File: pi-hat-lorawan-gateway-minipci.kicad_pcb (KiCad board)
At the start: 2 copper layers, 85 x 56 mm, 4 parts, among them Con1 RPi-Header-2x13, Con2 2041119-1

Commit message: Finalized project and generated all production files
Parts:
- added C1: 100n, Capacitors_Smd_0603:100nF_0603, F.Cu at (106.9, 109.5)
- added C2: 10uF, Capacitors_Smd_0603:10uF_10V_0603, F.Cu at (106.9, 106.9)
- added C3: 10uF, Capacitors_Smd_0603:10uF_10V_0603, F.Cu at (109.0, 77.6)
- added C4: 10uF, Capacitors_Smd_0603:10uF_10V_0603, F.Cu at (109.2, 83.4)
- added D1: KPG-1608SURKC-T, Diodes:LED_KPG-1608SURKC-T, F.Cu at (127.9, 81.8)
- added R3: 200R, Resistor_Smd_0603:200R_0603, F.Cu at (125.2, 81.8)
- added U1: LD39200, Linear:LD39200PU33R, F.Cu at (108.9, 80.5)
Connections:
- Con1 pad 10: (no net) -> /GPIO15(RXD)
- Con1 pad 11: (no net) -> /GPIO17(RTS)
- Con1 pad 12: (no net) -> /GPIO18(PWM)
- Con1 pad 13: (no net) -> /GPIO21
- Con1 pad 14: (no net) -> GND
- Con1 pad 15: (no net) -> /GPIO22
- Con1 pad 16: (no net) -> /GPIO23
- Con1 pad 17: (no net) -> 3V3
- Con1 pad 18: (no net) -> /GPIO24
- Con1 pad 19: (no net) -> /GPIO10(MOSI)
- Con1 pad 2: (no net) -> 5V
- Con1 pad 20: (no net) -> GND
- Con1 pad 21: (no net) -> /GPIO9(MISO)
- Con1 pad 22: (no net) -> /GPIO25
- Con1 pad 23: (no net) -> /GPIO11(SCLK)
- Con1 pad 24: (no net) -> /GPIO8(CE0)
- Con1 pad 25: (no net) -> GND
- Con1 pad 26: (no net) -> /GPIO7(CE1)
- Con1 pad 3: (no net) -> /GPIO0(SDA)
- Con1 pad 4: (no net) -> 5V
- Con1 pad 5: (no net) -> /GPIO1(SCL)
- Con1 pad 7: (no net) -> /GPIO4
- Con1 pad 8: (no net) -> /GPIO14(TXD)
- Con1 pad 9: (no net) -> GND
- Con2 pad 1: (no net) -> /GPIO4
- Con2 pad 10: (no net) -> /GPIO25
- Con2 pad 11: (no net) -> /GPIO14(TXD)
- Con2 pad 12: (no net) -> /GPIO10(MOSI)
- Con2 pad 13: (no net) -> /GPIO15(RXD)
- Con2 pad 14: (no net) -> /GPIO9(MISO)
- Con2 pad 16: (no net) -> /GPIO11(SCLK)
- Con2 pad 20: (no net) -> /GPIO8(CE0)
- Con2 pad 22: (no net) -> /GPIO22
- Con2 pad 23: (no net) -> /GPIO17(RTS)
- Con2 pad 25: (no net) -> /GPIO21
- Con2 pad 30: /MiniPci Express Module/I2C-SCL -> /GPIO1(SCL)
- Con2 pad 31: (no net) -> /GPIO18(PWM)
- Con2 pad 32: /MiniPci Express Module/I2C-SDA -> /GPIO0(SDA)
- Con2 pad 33: (no net) -> /GPIO7(CE1)
- Con2 pad 45: (no net) -> /GPIO23
- Con2 pad 8: (no net) -> /GPIO24
- R1 pad 2: /MiniPci Express Module/I2C-SCL -> /GPIO1(SCL)
- R2 pad 2: /MiniPci Express Module/I2C-SDA -> /GPIO0(SDA)
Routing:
- net 3V3: track 0.00 -> 107.1 mm, vias 0 -> 3
- net /GPIO7(CE1): track 0.00 -> 59.1 mm, vias 0 -> 2
- net /GPIO0(SDA): track 0.00 -> 52.6 mm, vias 0 -> 3
- net /GPIO1(SCL): track 0.00 -> 48.5 mm, vias 0 -> 3
- net /GPIO8(CE0): track 0.00 -> 46.6 mm, vias 0 -> 2
- net /GPIO23: track 0.00 -> 46.1 mm, vias 0 -> 2
- net /GPIO18(PWM): track 0.00 -> 38.5 mm
- net /GPIO25: track 0.00 -> 36.6 mm
- net /GPIO11(SCLK): track 0.00 -> 34.3 mm
- net /GPIO21: track 0.00 -> 33.9 mm, vias 0 -> 2
- net /GPIO9(MISO): track 0.00 -> 32.5 mm
- net /GPIO10(MOSI): track 0.00 -> 32.0 mm
- net /GPIO17(RTS): track 0.00 -> 31.9 mm
- net /GPIO22: track 0.00 -> 31.1 mm
- net /GPIO15(RXD): track 0.00 -> 28.1 mm, vias 0 -> 2
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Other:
- rule via_min_drill: 0.5 -> 0.4

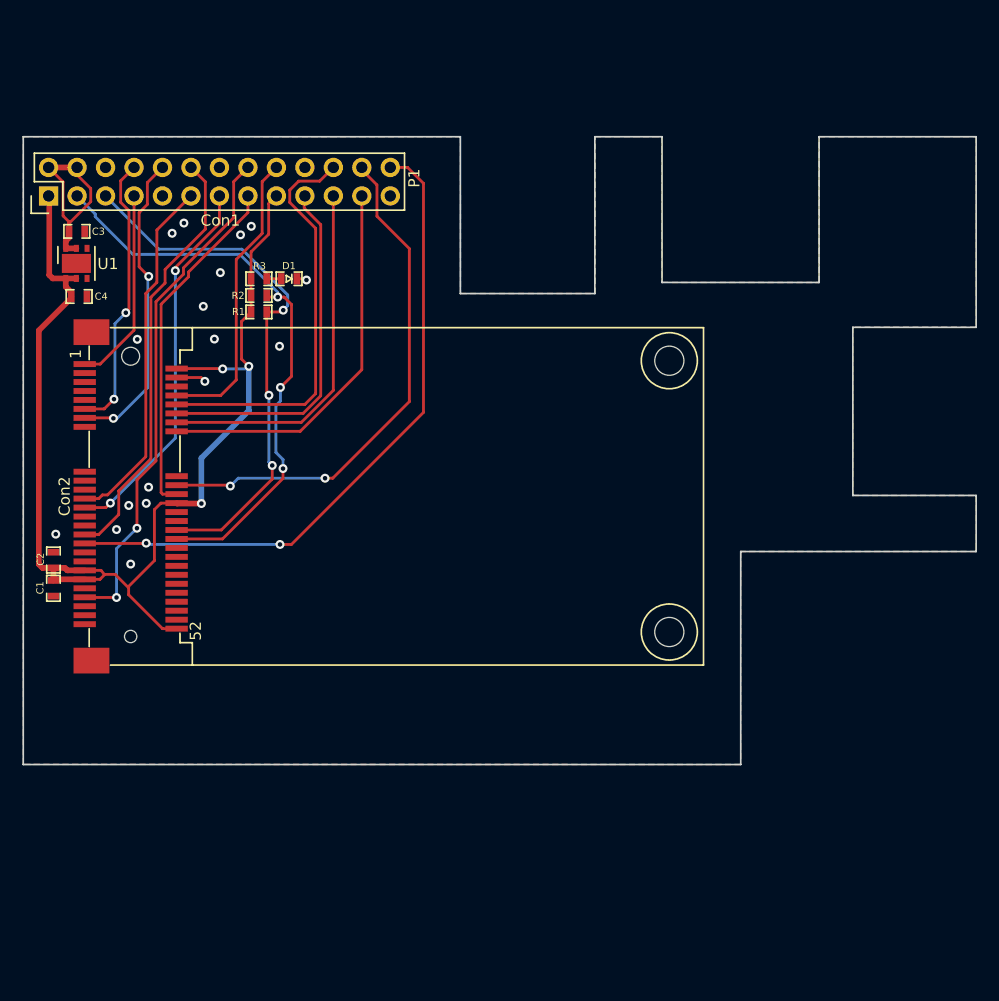
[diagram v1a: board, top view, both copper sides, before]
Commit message: Applied Issue 1, performed valid SPI connection to RPi
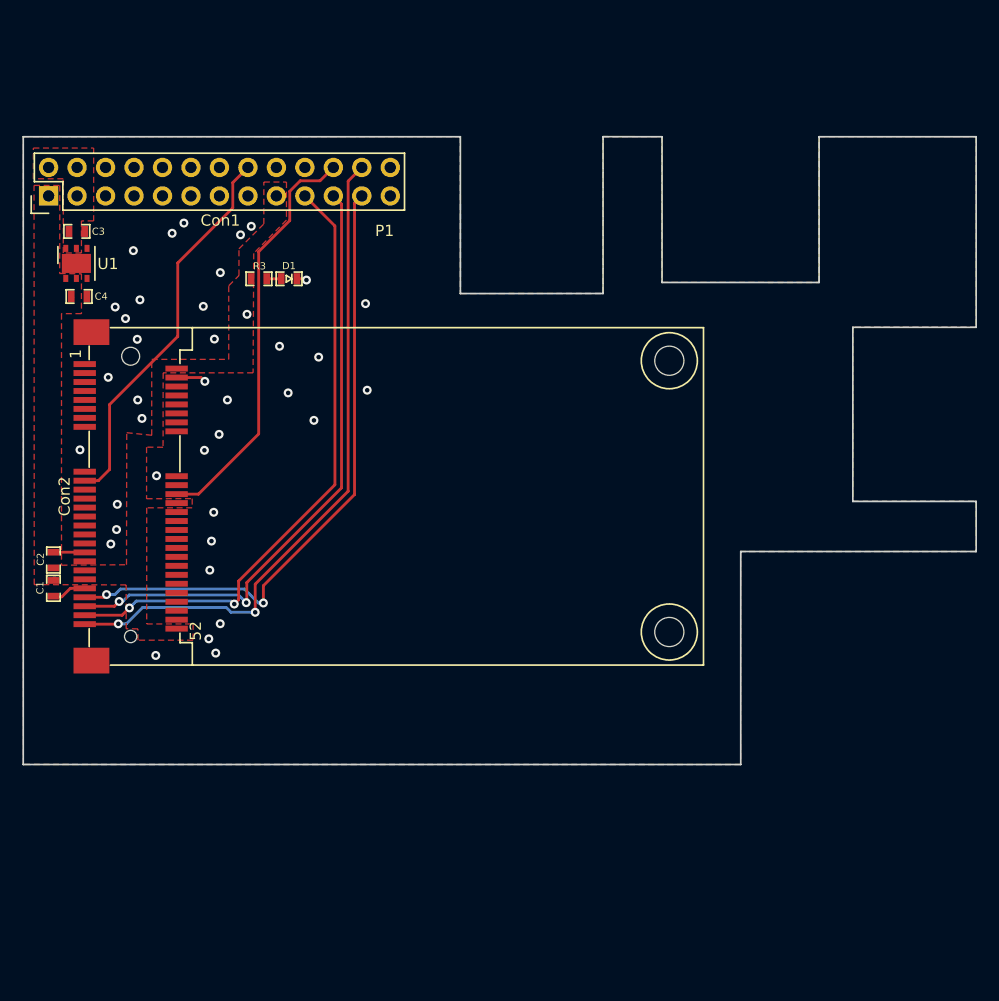
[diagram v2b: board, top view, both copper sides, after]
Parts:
- removed R1, R2: 4k7, Resistor_Smd_0603:4k7_0603
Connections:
- Con1 pad 10: /GPIO15(RXD) -> (no net)
- Con1 pad 11: /GPIO17(RTS) -> (no net)
- Con1 pad 12: /GPIO18(PWM) -> (no net)
- Con1 pad 13: /GPIO21 -> (no net)
- Con1 pad 15: /GPIO22 -> (no net)
- Con1 pad 18: /GPIO24 -> (no net)
- Con1 pad 26: /GPIO7(CE1) -> (no net)
- Con1 pad 7: /GPIO4 -> (no net)
- Con1 pad 8: /GPIO14(TXD) -> (no net)
- Con2 pad 1: /GPIO4 -> (no net)
- Con2 pad 10: /GPIO25 -> (no net)
- Con2 pad 11: /GPIO14(TXD) -> (no net)
- Con2 pad 12: /GPIO10(MOSI) -> (no net)
- Con2 pad 13: /GPIO15(RXD) -> (no net)
- Con2 pad 14: /GPIO9(MISO) -> (no net)
- Con2 pad 16: /GPIO11(SCLK) -> (no net)
- Con2 pad 19: (no net) -> /GPIO23
- Con2 pad 20: /GPIO8(CE0) -> GND
- Con2 pad 22: /GPIO22 -> /GPIO25
- Con2 pad 23: /GPIO17(RTS) -> (no net)
- Con2 pad 25: /GPIO21 -> (no net)
- Con2 pad 30: /GPIO1(SCL) -> (no net)
- Con2 pad 31: /GPIO18(PWM) -> (no net)
- Con2 pad 32: /GPIO0(SDA) -> (no net)
- Con2 pad 33: /GPIO7(CE1) -> (no net)
- Con2 pad 45: /GPIO23 -> /GPIO11(SCLK)
- Con2 pad 47: (no net) -> /GPIO9(MISO)
- Con2 pad 49: (no net) -> /GPIO10(MOSI)
- Con2 pad 51: (no net) -> /GPIO8(CE0)
- Con2 pad 8: /GPIO24 -> (no net)
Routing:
- net 3V3: track 107.1 -> 0.37 mm, vias 3 -> 0
- net /GPIO7(CE1): track 59.1 -> 0.00 mm, vias 2 -> 0
- net /GPIO0(SDA): track 52.6 -> 0.00 mm, vias 3 -> 0
- net /GPIO1(SCL): track 48.5 -> 0.00 mm, vias 3 -> 0
- net /GPIO18(PWM): track 38.5 -> 0.00 mm
- net /GPIO21: track 33.9 -> 0.00 mm, vias 2 -> 0
- net /GPIO17(RTS): track 31.9 -> 0.00 mm
- net /GPIO22: track 31.1 -> 0.00 mm
- net /GPIO15(RXD): track 28.1 -> 0.00 mm, vias 2 -> 0
- net /GPIO24: track 26.3 -> 0.00 mm
- net /GPIO14(TXD): track 25.0 -> 0.00 mm, vias 2 -> 0
- net /GPIO10(MOSI): track 32.0 -> 55.3 mm, vias 0 -> 2
- net /GPIO9(MISO): track 32.5 -> 55.2 mm, vias 0 -> 2
- net /GPIO11(SCLK): track 34.3 -> 56.7 mm, vias 0 -> 2
- net /GPIO4: track 17.6 -> 0.00 mm
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- added copper zone on F.Cu, net 3V3
- added copper zone on F.Cu, net 5V
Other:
- outline, holes or cut-outs redrawn
- net class Default removed
- net class Power removed

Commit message: Board revorked to RPI-4 Hat Vertical
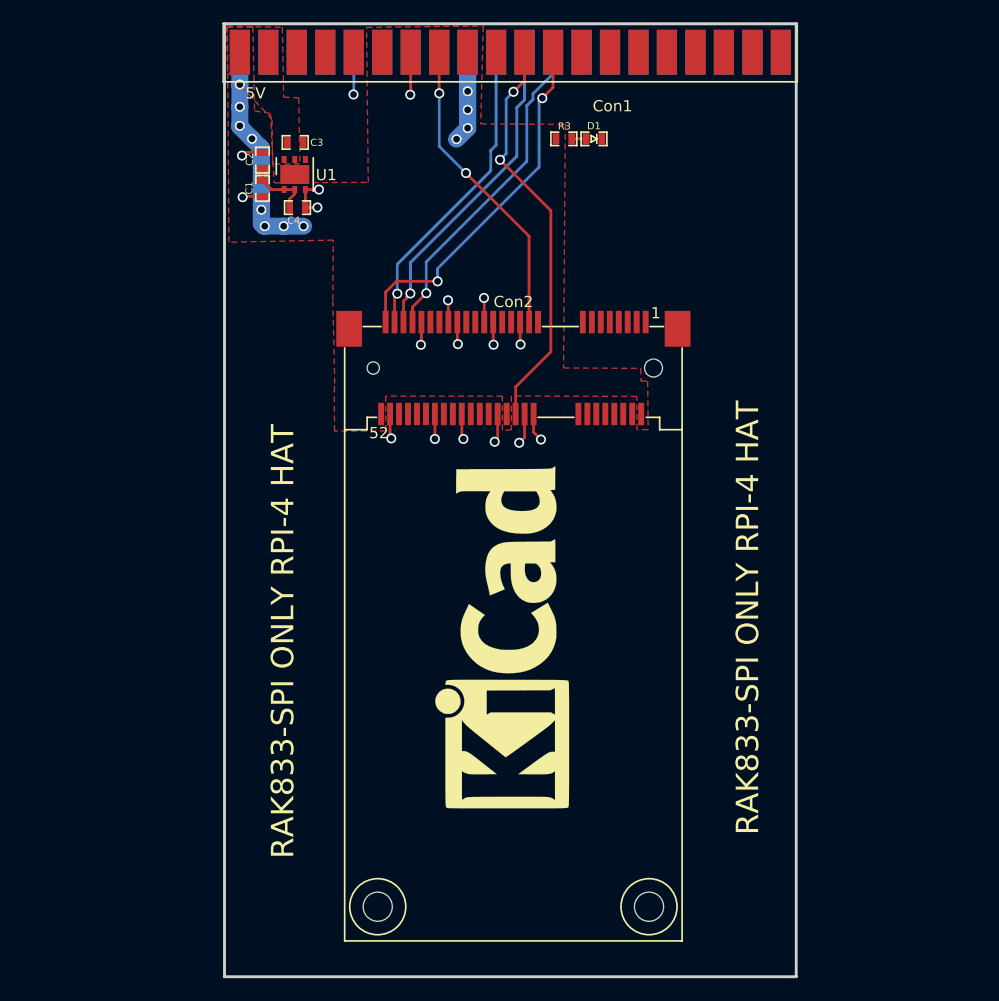
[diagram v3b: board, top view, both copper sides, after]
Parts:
- added REF**: KiCad-Logo_12mm_SilkScreen, Symbols:KiCad-Logo_12mm_SilkScreen, F.Cu at (146.9, 113.8)
- added REF**: OSHW-Symbol_33.5x30mm_SilkScreen, Symbols:OSHW-Symbol_33.5x30mm_SilkScreen, B.Cu at (148.5, 104.6)
- Con1: value RPi-Header-2x13 -> Header_Socket_2x20pin; footprint Header_Socket_2_54mm:Header_Socket_2x13x2_54mm -> Header_Socket_2_54mm:Header_Socket_Vertical_2x20x2_54mm
- moved C1 40.3 mm to (125.5, 73.8)
- moved C2 40.3 mm to (125.5, 71.3)
- moved Con2 36.0 mm to (147.9, 89.8), turned to 180 degrees
- moved R3 29.9 mm to (152.4, 69.4)
- moved D1 29.9 mm to (155.1, 69.4)
- moved Con1 29.5 mm to (147.6, 59.1)
- moved C4 21.0 mm to (128.7, 75.5)
- moved C3 21.0 mm to (128.4, 69.7)
- moved U1 21.0 mm to (128.4, 72.5)
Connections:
- Con1 pad 1: 3V3 -> 5V
- Con1 pad 10: (no net) -> GND
- Con1 pad 13: (no net) -> GND
- Con1 pad 14: GND -> (no net)
- Con1 pad 15: (no net) -> /GPIO23
- Con1 pad 16: /GPIO23 -> (no net)
- Con1 pad 17: 3V3 -> (no net)
- Con1 pad 18: (no net) -> 3V3
- Con1 pad 19: /GPIO10(MOSI) -> GND
- Con1 pad 2: 5V -> 3V3
- Con1 pad 20: GND -> /GPIO10(MOSI)
- Con1 pad 21: /GPIO9(MISO) -> /GPIO25
- Con1 pad 22: /GPIO25 -> /GPIO9(MISO)
- Con1 pad 23: /GPIO11(SCLK) -> /GPIO8(CE0)
- Con1 pad 24: /GPIO8(CE0) -> /GPIO11(SCLK)
- Con1 pad 25: GND -> (no net)
- Con1 pad 26: (no net) -> GND
- Con1 pad 3: /GPIO0(SDA) -> 5V
- Con1 pad 4: 5V -> (no net)
- Con1 pad 5: /GPIO1(SCL) -> GND
- Con1 pad 6: GND -> (no net)
- Con1 pad 9: GND -> (no net)
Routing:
- net 3V3: track 0.37 -> 34.2 mm, vias 0 -> 12
- net GND: track 9.49 -> 42.1 mm, vias 39 -> 18
- net /GPIO10(MOSI): track 55.3 -> 27.8 mm, vias 2 -> 1
- net /GPIO11(SCLK): track 56.7 -> 29.3 mm, vias 2 -> 1
- net /GPIO8(CE0): track 59.8 -> 32.4 mm
- net /GPIO9(MISO): track 55.2 -> 28.5 mm, vias 2 -> 1
- net /GPIO23: track 34.7 -> 27.4 mm, vias 0 -> 2
- net 5V: track 1.23 -> 0.00 mm
- net /GPIO25: track 37.1 -> 36.4 mm, vias 0 -> 2
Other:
- board size 85 x 56 mm -> 51 x 85 mm
- board text added: "5V"
- board text added: "RAK833-SPI ONLY RPI-4 HAT"

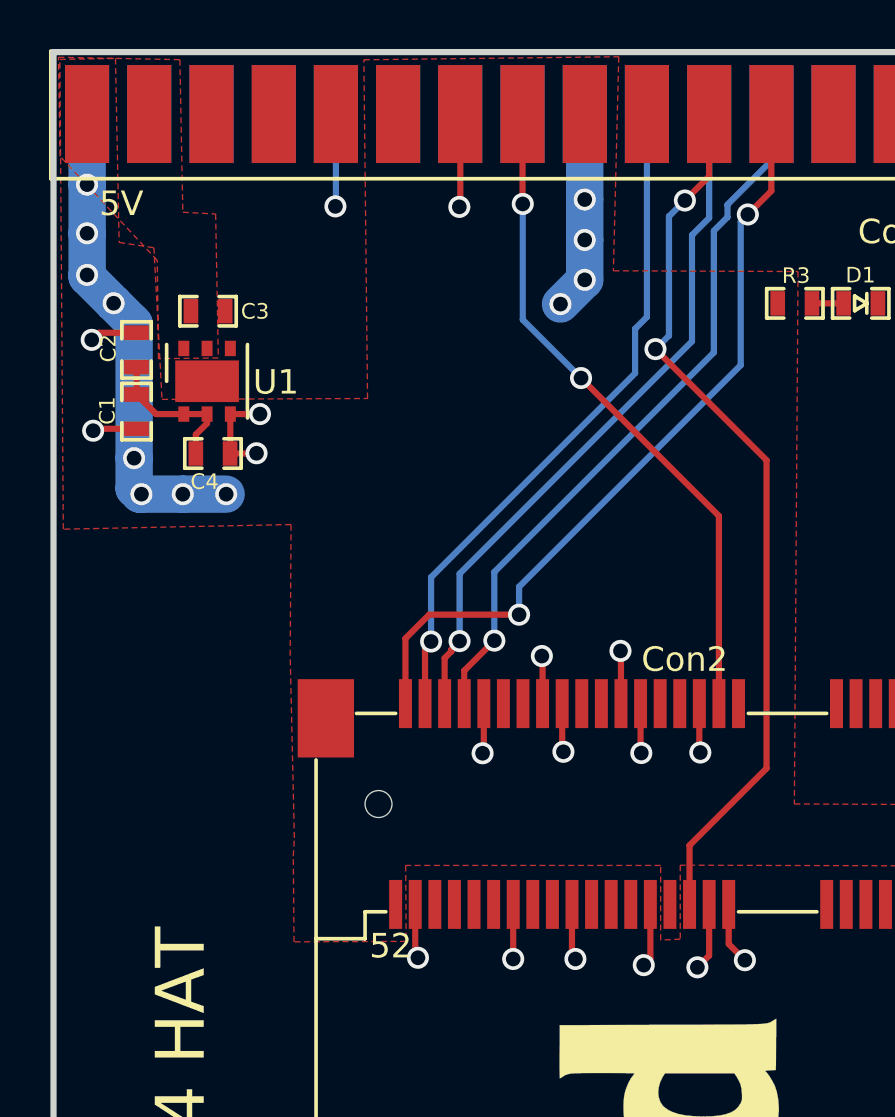
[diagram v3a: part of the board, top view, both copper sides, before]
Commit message: Applied issue and regenerated gerbers
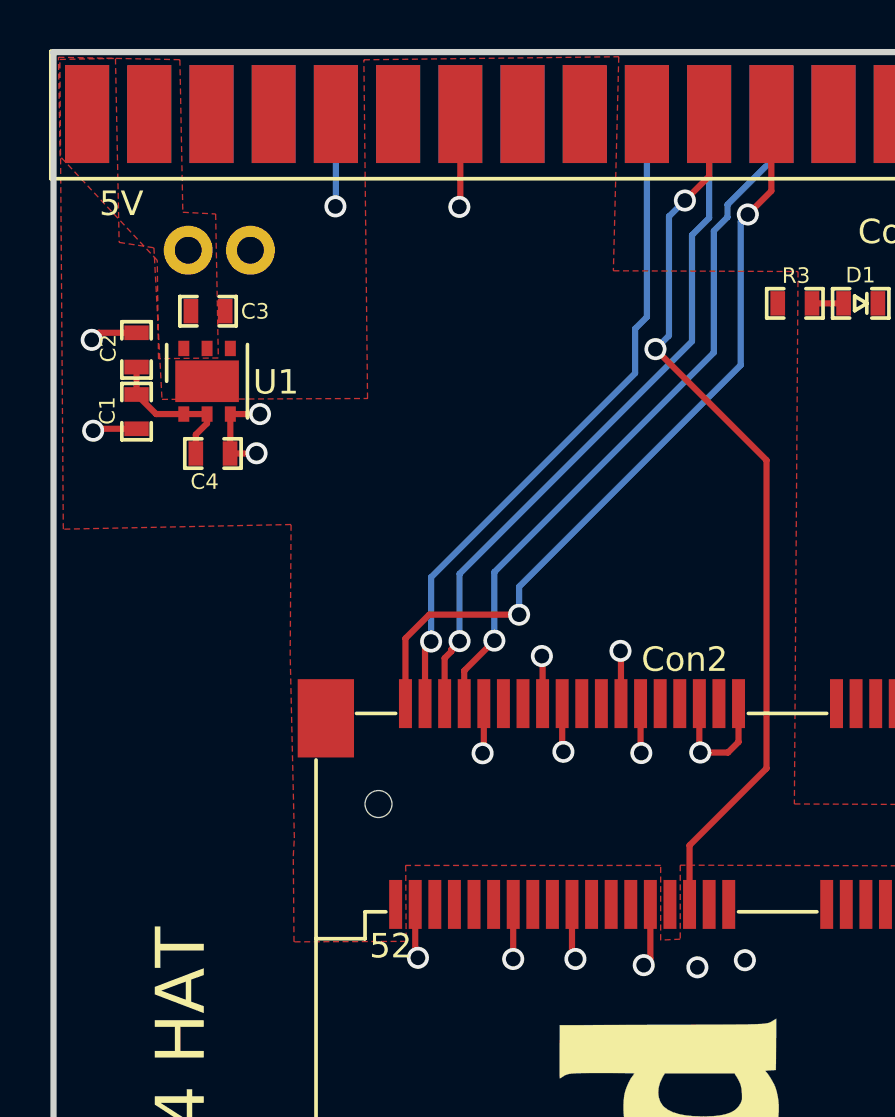
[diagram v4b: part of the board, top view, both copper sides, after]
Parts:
- added P1: RPI4 Cooler, Goldpin:Goldpin_2_2_54mm_90deg, B.Cu at (128.9, 69.9)
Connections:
- Con1 pad 15: /GPIO23 -> (no net)
- Con1 pad 18: 3V3 -> (no net)
- Con1 pad 2: 3V3 -> (no net)
- Con2 pad 17: (no net) -> GND
- Con2 pad 18: GND -> (no net)
- Con2 pad 19: /GPIO23 -> (no net)
- Con2 pad 20: GND -> (no net)
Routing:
- net 3V3: track 34.2 -> 6.13 mm, vias 12 -> 0
- net /GPIO23: track 27.4 -> 0.00 mm, vias 2 -> 0
- net GND: track 42.1 -> 40.1 mm
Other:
- board text added: "GND"
